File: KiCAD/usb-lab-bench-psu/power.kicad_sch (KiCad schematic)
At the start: 1 part

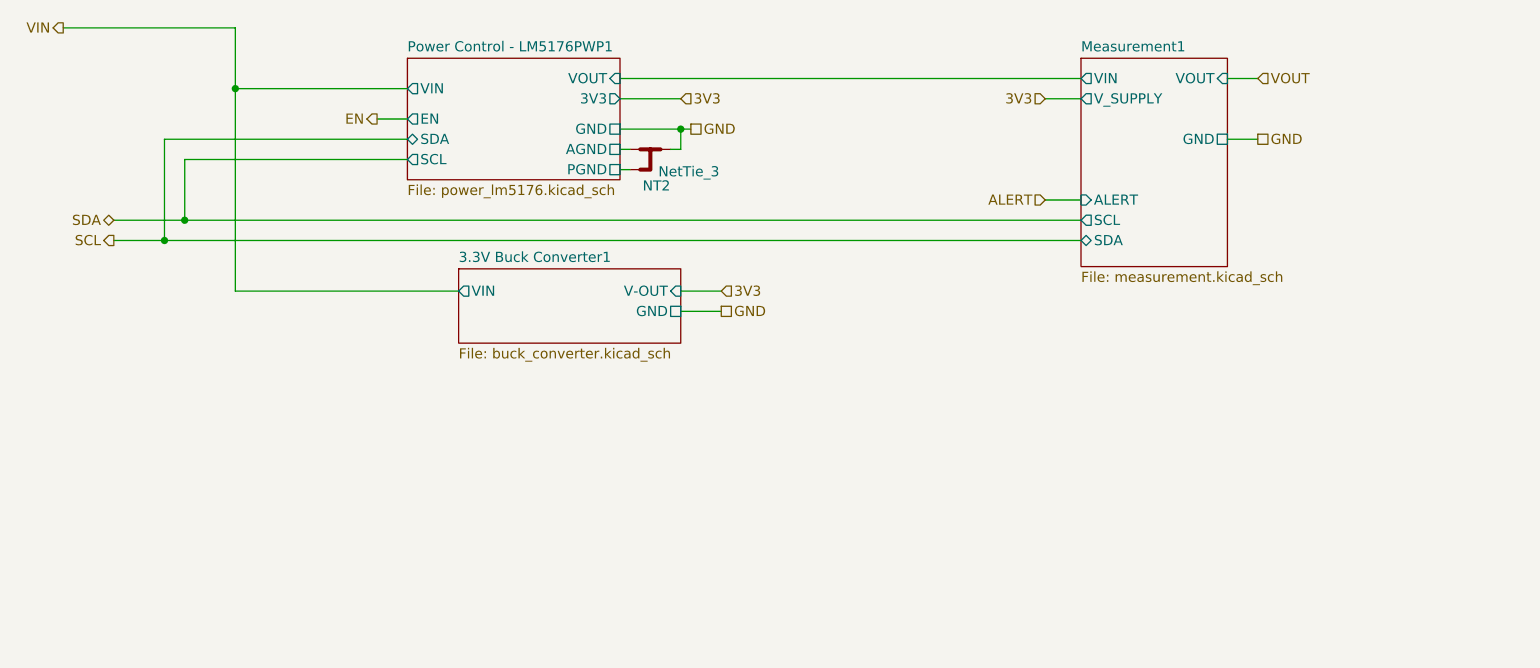
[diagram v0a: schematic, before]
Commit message: added current limiting circuit for USB PD sink, added 2nd buck converter
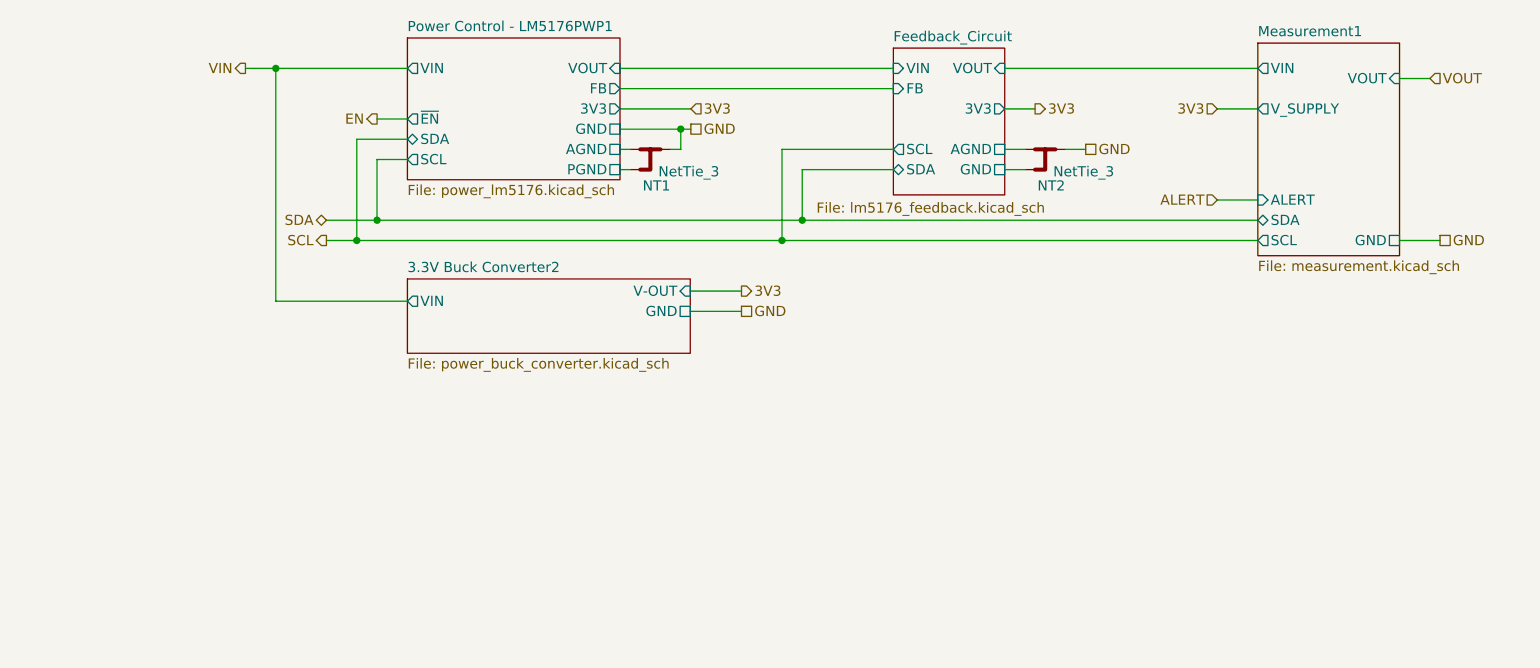
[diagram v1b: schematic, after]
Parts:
- added NT2: NetTie_3, symbol Device:NetTie_3
- renumbered NT2 to NT1
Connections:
- net GND: now also NT2.2
- new net Feedback_Circuit/AGND: NT2.1
- new net Feedback_Circuit/GND: NT2.3
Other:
- removed sheet 3.3V Buck Converter1
- added sheet 3.3V Buck Converter2 (power_buck_converter.kicad_sch)
- added sheet Feedback_Circuit (lm5176_feedback.kicad_sch)
- sheet Power Control - LM5176PWP1 ports: added FB, ~{EN}; removed EN

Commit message: Fixed label directions
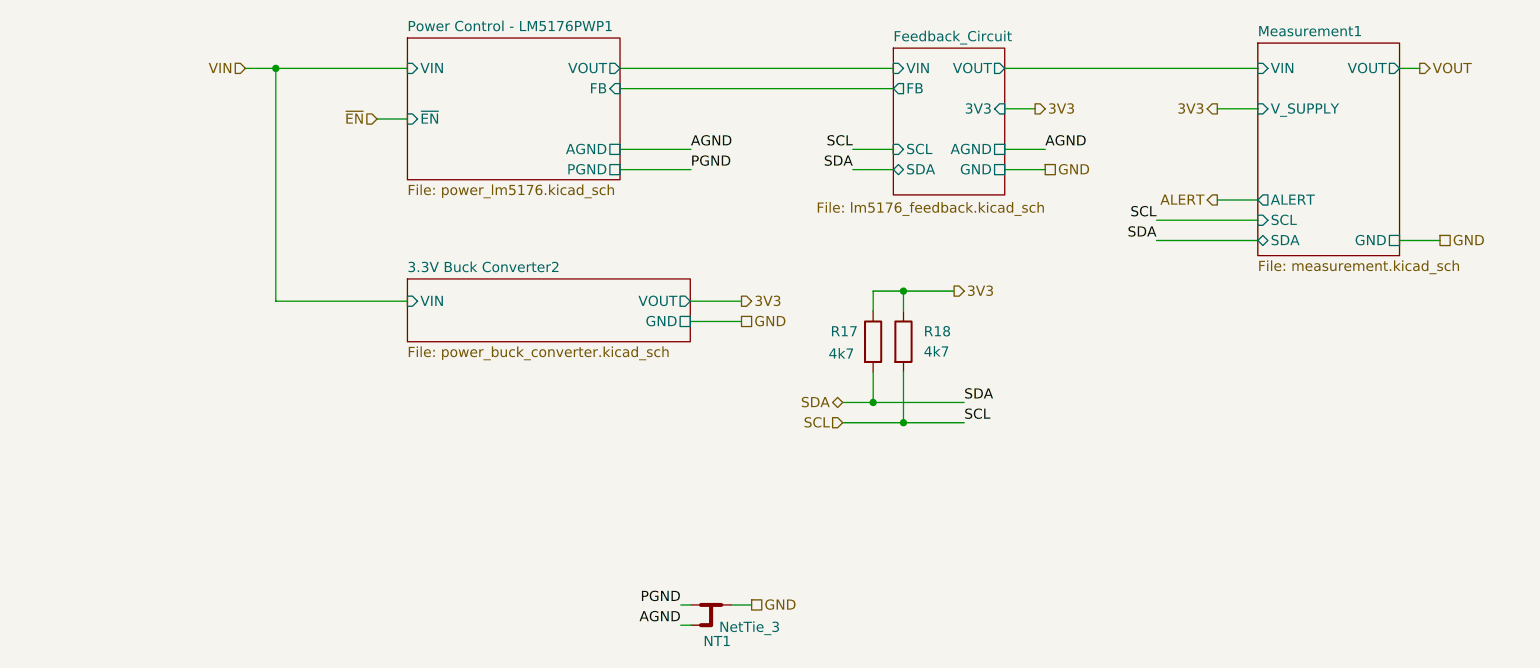
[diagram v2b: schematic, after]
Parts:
- removed NT2: NetTie_3, symbol Device:NetTie_3
- added R17, R18: 4k7, symbol Device:R
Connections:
- net 3V3: now also R17.1, R18.1
- net SCL: now also R18.2
- net SDA: now also R17.2
- net Power Control - LM5176PWP1/AGND renamed PGND
- net Power Control - LM5176PWP1/PGND renamed AGND
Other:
- sheet 3.3V Buck Converter2 ports: added VOUT; removed V-OUT
- sheet Power Control - LM5176PWP1 ports: added none; removed 3V3, GND, SCL, SDA
- moved on the sheet: NT1
